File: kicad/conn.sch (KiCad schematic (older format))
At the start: 2 parts, among them J1704 idc2x17, J1705 idc2x17

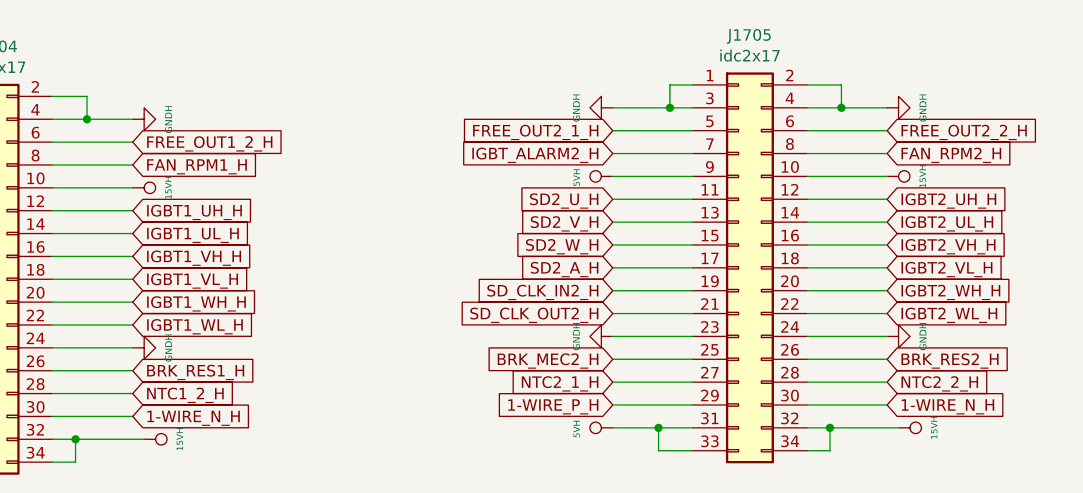
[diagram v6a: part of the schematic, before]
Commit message: roouting and more routing.... I think 4 layers WONT be enought
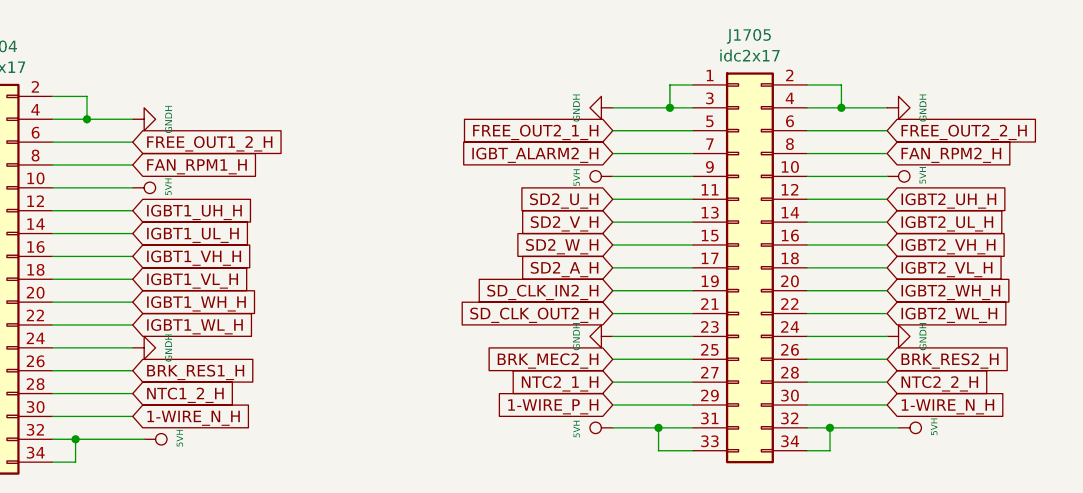
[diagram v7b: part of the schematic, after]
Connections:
- net 15VH is gone; now on net 5VH: J1704.10 (Pin_10), J1704.32 (Pin_32), J1704.34 (Pin_34), J1705.10 (Pin_10), J1705.32 (Pin_32), J1705.34 (Pin_34)
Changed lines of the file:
@@
 	0    -1   1    0
-$EndComp
-$Comp
-L servo:15VH #PWR?
-U 1 1 5E7CE3D5
-P 10550 2600
-AR Path="/5DDE8C5E/5E7CE3D5" Ref="#PWR?"  Part="1"
-AR Path="/5EC40F3C/5E7CE3D5" Ref="#PWR0274"  Part="1"
-F 0 "#PWR0274" H 10550 2400 20  0001 C CNN
-F 1 "15VH" H 10550 2757 28  0000 C CNN
-F 2 "" H 10550 2600 50  0001 C CNN
-F 3 "" H 10550 2600 50  0001 C CNN
-	1    10550 2600
-	0    1    1    0
 $EndComp
 Wire Wire Line
@@
 Wire Wire Line
 	10200 2300 10350 2300
-$Comp
-L servo:15VH #PWR?
-U 1 1 5E7CE40B
-P 10600 3700
-AR Path="/5DDE8C5E/5E7CE40B" Ref="#PWR?"  Part="1"
-AR Path="/5EC40F3C/5E7CE40B" Ref="#PWR0278"  Part="1"
-F 0 "#PWR0278" H 10600 3500 20  0001 C CNN
-F 1 "15VH" H 10600 3857 28  0000 C CNN
-F 2 "" H 10600 3700 50  0001 C CNN
-F 3 "" H 10600 3700 50  0001 C CNN
-	1    10600 3700
-	0    1    1    0
-$EndComp
 $Comp
 L servo:5VH #PWR?
@@
 	0    -1   1    0
 $EndComp
-$Comp
-L servo:15VH #PWR?
-U 1 1 5E970324
-P 7250 2650
-AR Path="/5DDE8C5E/5E970324" Ref="#PWR?"  Part="1"
-AR Path="/5EC40F3C/5E970324" Ref="#PWR01707"  Part="1"
-F 0 "#PWR01707" H 7250 2450 20  0001 C CNN
-F 1 "15VH" H 7250 2807 28  0000 C CNN
-F 2 "" H 7250 2650 50  0001 C CNN
-F 3 "" H 7250 2650 50  0001 C CNN
-	1    7250 2650
-	0    1    1    0
-$EndComp
 Wire Wire Line
 	6050 3550 6400 3550
@@
 Wire Wire Line
 	6900 2350 7050 2350
-$Comp
-L servo:15VH #PWR?
-U 1 1 5E970347
-P 7300 3750
-AR Path="/5DDE8C5E/5E970347" Ref="#PWR?"  Part="1"
-AR Path="/5EC40F3C/5E970347" Ref="#PWR01709"  Part="1"
-F 0 "#PWR01709" H 7300 3550 20  0001 C CNN
-F 1 "15VH" H 7300 3907 28  0000 C CNN
-F 2 "" H 7300 3750 50  0001 C CNN
-F 3 "" H 7300 3750 50  0001 C CNN
-	1    7300 3750
-	0    1    1    0
-$EndComp
 $Comp
 L servo:5VH #PWR?
@@
 Text GLabel 10550 3200 2    50   Input ~ 0
 IGBT2_WL_H
+$Comp
+L servo:5VH #PWR?
+U 1 1 5E2DC544
+P 7300 3750
+AR Path="/5DDE8C5E/5E2DC544" Ref="#PWR?"  Part="1"
+AR Path="/5EC40F3C/5E2DC544" Ref="#PWR0145"  Part="1"
+F 0 "#PWR0145" H 7300 3550 20  0001 C CNN
+F 1 "5VH" H 7305 3907 28  0000 C CNN
+F 2 "" H 7300 3750 50  0001 C CNN
+F 3 "" H 7300 3750 50  0001 C CNN
+	1    7300 3750
+	0    1    -1   0
+$EndComp
+$Comp
+L servo:5VH #PWR?
+U 1 1 5E2E3CB8
+P 7250 2650
+AR Path="/5DDE8C5E/5E2E3CB8" Ref="#PWR?"  Part="1"
+AR Path="/5EC40F3C/5E2E3CB8" Ref="#PWR0270"  Part="1"
+F 0 "#PWR0270" H 7250 2450 20  0001 C CNN
+F 1 "5VH" H 7255 2807 28  0000 C CNN
+F 2 "" H 7250 2650 50  0001 C CNN
+F 3 "" H 7250 2650 50  0001 C CNN
+	1    7250 2650
+	0    1    -1   0
+$EndComp
+$Comp
+L servo:5VH #PWR?
+U 1 1 5E2E3D03
+P 10550 2600
+AR Path="/5DDE8C5E/5E2E3D03" Ref="#PWR?"  Part="1"
+AR Path="/5EC40F3C/5E2E3D03" Ref="#PWR0271"  Part="1"
+F 0 "#PWR0271" H 10550 2400 20  0001 C CNN
+F 1 "5VH" H 10555 2757 28  0000 C CNN
+F 2 "" H 10550 2600 50  0001 C CNN
+F 3 "" H 10550 2600 50  0001 C CNN
+	1    10550 2600
+	0    1    -1   0
+$EndComp
+$Comp
+L servo:5VH #PWR?
+U 1 1 5E2E3D37
+P 10600 3700
+AR Path="/5DDE8C5E/5E2E3D37" Ref="#PWR?"  Part="1"
+AR Path="/5EC40F3C/5E2E3D37" Ref="#PWR0274"  Part="1"
+F 0 "#PWR0274" H 10600 3500 20  0001 C CNN
+F 1 "5VH" H 10605 3857 28  0000 C CNN
+F 2 "" H 10600 3700 50  0001 C CNN
+F 3 "" H 10600 3700 50  0001 C CNN
+	1    10600 3700
+	0    1    -1   0
+$EndComp
 $EndSCHEMATC
